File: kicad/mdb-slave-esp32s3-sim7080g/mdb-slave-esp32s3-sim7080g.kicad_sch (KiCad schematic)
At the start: 81 parts, among them J1 USB_C_Receptacle_USB2.0_16P, J2 JAE_SIM_Card_SF72S006, J3 Conn_01x03_Pin, J4 Conn_Coaxial, J5 Conn_Coaxial, J6 MDB_Connector, J7 Conn_01x03_Pin, J8 Conn_01x04_Pin, Q1 MMBT3904, Q2 MMBT3904, Q3 MMBT3904, Q4 MMBT3904, Q5 MMBT3904, Q6 MMBT3904, Q7 MMBT3904, SW1 SW_Push, U1 ESP32-S3FH4R2, U2 SIM7080G, U3 LM2594HVM-3.3, U4 TLP785, U5 TLP785, Y1 Crystal_GND24

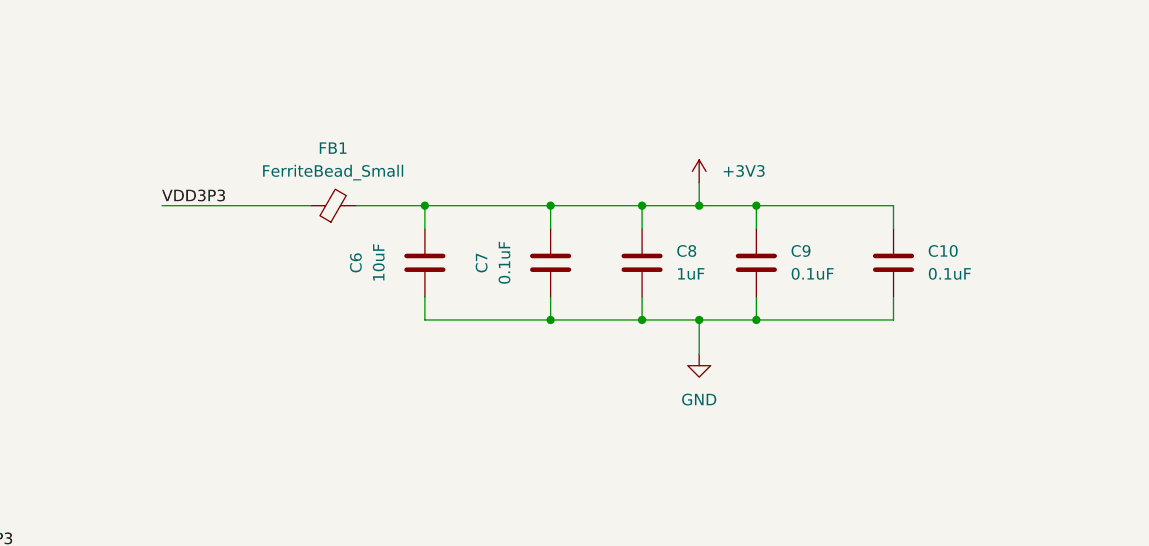
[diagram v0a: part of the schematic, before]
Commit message: moving capacitor 0.1uf to left ferrite bead
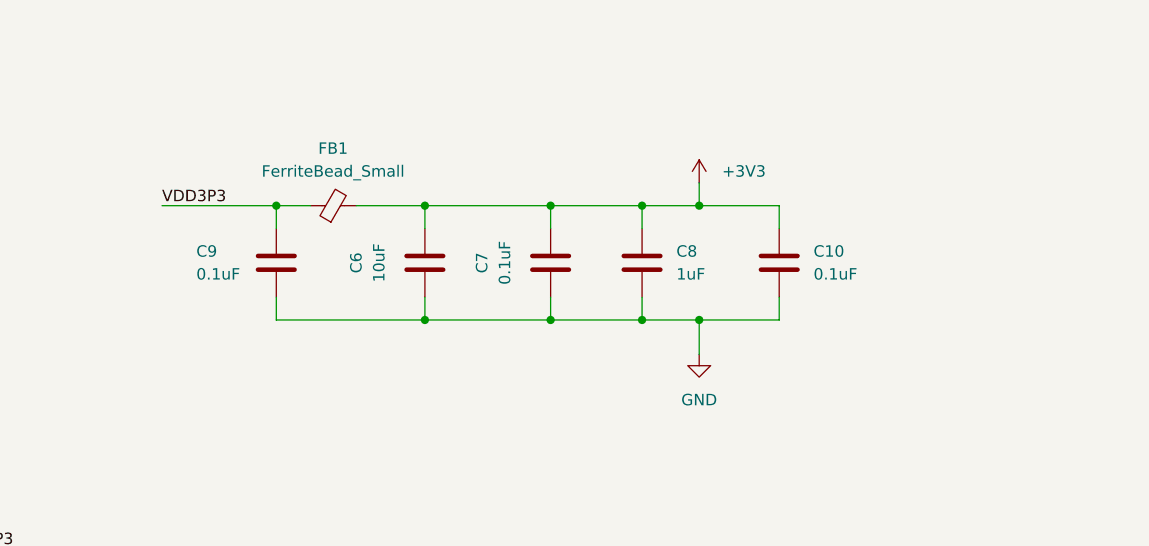
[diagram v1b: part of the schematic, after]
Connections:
- net +3V3: no longer C9.1
- net VDD3P3: now also C9.1
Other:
- moved on the sheet: C10, C9
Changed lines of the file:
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@@
 	)
 	(junction
-		(at 209.55 60.96)
-		(diameter 0)
-		(color 0 0 0 0)
-	)
-	(junction
 		(at 252.73 270.51)
 		(diameter 0)
@@
 	)
 	(junction
+		(at 172.72 60.96)
+		(diameter 0)
+		(color 0 0 0 0)
+	)
+	(junction
 		(at 81.28 133.35)
 		(diameter 0)
@@
 	)
 	(junction
-		(at 209.55 48.26)
-		(diameter 0)
-		(color 0 0 0 0)
-	)
-	(junction
 		(at 219.71 148.59)
 		(diameter 0)
@@
 	)
 	(junction
+		(at 156.21 48.26)
+		(diameter 0)
+		(color 0 0 0 0)
+	)
+	(junction
 		(at 63.5 123.19)
 		(diameter 0)
@@
 	(wire
 		(pts
-			(xy 224.79 48.26) (xy 224.79 50.8)
+			(xy 212.09 48.26) (xy 212.09 50.8)
 		)
 		(stroke
@@
 	(wire
 		(pts
-			(xy 209.55 60.96) (xy 224.79 60.96)
-		)
-		(stroke
-			(width 0)
-			(type default)
-		)
-	)
-	(wire
-		(pts
 			(xy 297.18 306.07) (xy 294.64 306.07)
 		)
@@
 	(wire
 		(pts
-			(xy 143.51 48.26) (xy 160.02 48.26)
+			(xy 143.51 48.26) (xy 156.21 48.26)
 		)
 		(stroke
@@
 	(wire
 		(pts
-			(xy 209.55 50.8) (xy 209.55 48.26)
+			(xy 156.21 48.26) (xy 156.21 50.8)
 		)
 		(stroke
@@
 	(wire
 		(pts
+			(xy 156.21 60.96) (xy 172.72 60.96)
+		)
+		(stroke
+			(width 0)
+			(type default)
+		)
+	)
+	(wire
+		(pts
 			(xy 81.28 147.32) (xy 81.28 144.78)
 		)
@@
 	(wire
 		(pts
+			(xy 156.21 58.42) (xy 156.21 60.96)
+		)
+		(stroke
+			(width 0)
+			(type default)
+		)
+	)
+	(wire
+		(pts
 			(xy 426.72 57.15) (xy 416.56 57.15)
 		)
@@
 	(wire
 		(pts
-			(xy 209.55 60.96) (xy 209.55 58.42)
-		)
-		(stroke
-			(width 0)
-			(type default)
-		)
-	)
-	(wire
-		(pts
 			(xy 26.67 109.22) (xy 26.67 115.57)
 		)
@@
 	(wire
 		(pts
-			(xy 203.2 60.96) (xy 209.55 60.96)
+			(xy 203.2 60.96) (xy 212.09 60.96)
 		)
 		(stroke
@@
 	(wire
 		(pts
+			(xy 156.21 48.26) (xy 160.02 48.26)
+		)
+		(stroke
+			(width 0)
+			(type default)
+		)
+	)
+	(wire
+		(pts
 			(xy 425.45 149.86) (xy 436.88 149.86)
 		)
@@
 	(wire
 		(pts
-			(xy 224.79 60.96) (xy 224.79 58.42)
+			(xy 212.09 60.96) (xy 212.09 58.42)
 		)
 		(stroke
@@
 	(wire
 		(pts
-			(xy 209.55 48.26) (xy 224.79 48.26)
-		)
-		(stroke
-			(width 0)
-			(type default)
-		)
-	)
-	(wire
-		(pts
 			(xy 105.41 243.84) (xy 105.41 248.92)
 		)
@@
 	(wire
 		(pts
-			(xy 203.2 48.26) (xy 209.55 48.26)
+			(xy 203.2 48.26) (xy 212.09 48.26)
 		)
 		(stroke
@@
 	(symbol
 		(lib_id "Device:C")
-		(at 224.79 54.61 0)
+		(at 212.09 54.61 0)
 		(unit 1)
 		(exclude_from_sim no)
@@
 		(fields_autoplaced yes)
 		(property "Reference" "C10"
-			(at 228.6 53.3399 0)
+			(at 215.9 53.3399 0)
 			(effects
 				(font
@@
 		)
 		(property "Value" "0.1uF"
-			(at 228.6 55.8799 0)
+			(at 215.9 55.8799 0)
 			(effects
 				(font
@@
 		)
 		(property "Footprint" "Capacitor_SMD:C_0603_1608Metric"
-			(at 225.7552 58.42 0)
+			(at 213.0552 58.42 0)
 			(effects
 				(font
@@
 		)
 		(property "Datasheet" "~"
-			(at 224.79 54.61 0)
+			(at 212.09 54.61 0)
 			(effects
 				(font
@@
 		)
 		(property "Description" ""
-			(at 224.79 54.61 0)
+			(at 212.09 54.61 0)
 			(effects
 				(font
@@
 		)
 		(property "LCSC#" "C5137636"
-			(at 224.79 54.61 90)
+			(at 212.09 54.61 90)
 			(effects
 				(font
@@
 		)
 		(property "Sim.Device" ""
-			(at 224.79 54.61 90)
+			(at 212.09 54.61 90)
 			(effects
 				(font
@@
 		)
 		(property "Sim.Pins" ""
-			(at 224.79 54.61 90)
+			(at 212.09 54.61 90)
 			(effects
 				(font
@@
 		)
 		(property "Sim.Type" ""
-			(at 224.79 54.61 90)
+			(at 212.09 54.61 90)
 			(effects
 				(font
@@
 	(symbol
 		(lib_id "Device:C")
-		(at 209.55 54.61 0)
+		(at 156.21 54.61 0)
 		(unit 1)
 		(exclude_from_sim no)
@@
 		(on_board yes)
 		(dnp no)
-		(fields_autoplaced yes)
 		(property "Reference" "C9"
-			(at 213.36 53.3399 0)
+			(at 147.32 53.34 0)
 			(effects
 				(font
@@
 		)
 		(property "Value" "0.1uF"
-			(at 213.36 55.8799 0)
+			(at 147.32 55.88 0)
 			(effects
 				(font
@@
 		)
 		(property "Footprint" "Capacitor_SMD:C_0603_1608Metric"
-			(at 210.5152 58.42 0)
+			(at 157.1752 58.42 0)
 			(effects
 				(font
@@
 		)
 		(property "Datasheet" "~"
-			(at 209.55 54.61 0)
+			(at 156.21 54.61 0)
 			(effects
 				(font
@@
 		)
 		(property "Description" ""
-			(at 209.55 54.61 0)
+			(at 156.21 54.61 0)
 			(effects
 				(font
@@
 		)
 		(property "LCSC#" "C5137636"
-			(at 209.55 54.61 90)
+			(at 156.21 54.61 90)
 			(effects
 				(font
@@
 		)
 		(property "Sim.Device" ""
-			(at 209.55 54.61 90)
+			(at 156.21 54.61 90)
 			(effects
 				(font
@@
 		)
 		(property "Sim.Pins" ""
-			(at 209.55 54.61 90)
+			(at 156.21 54.61 90)
 			(effects
 				(font
@@
 		)
 		(property "Sim.Type" ""
-			(at 209.55 54.61 90)
+			(at 156.21 54.61 90)
 			(effects
 				(font

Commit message: initial updates
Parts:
- removed R27: 4K7, Resistor_SMD:R_0603_1608Metric, symbol Device:R
- added Q9: MMBT3904, Package_TO_SOT_SMD:SOT-23, symbol Transistor_BJT:MMBT3904
- added R26, R29: 1k, Resistor_SMD:R_0603_1608Metric, symbol Device:R
- added R28, R30: 10k, Resistor_SMD:R_0603_1608Metric, symbol Device:R
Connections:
- net +3V3: now also R29.1, R30.2
- net GND: now also R28.1
- net io13: now also R26.2
- net io6: now also Q9.3 (C), R29.2
- net at Q7.1 (B): now also R26.1, R28.2
- net pulse: now reaches J7.3 (Pin_3), Q7.3 (C)
- net pulse: now also Q9.2 (E)
- new net: Q9.1 (B), R30.1
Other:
- moved on the sheet: J7, Q7

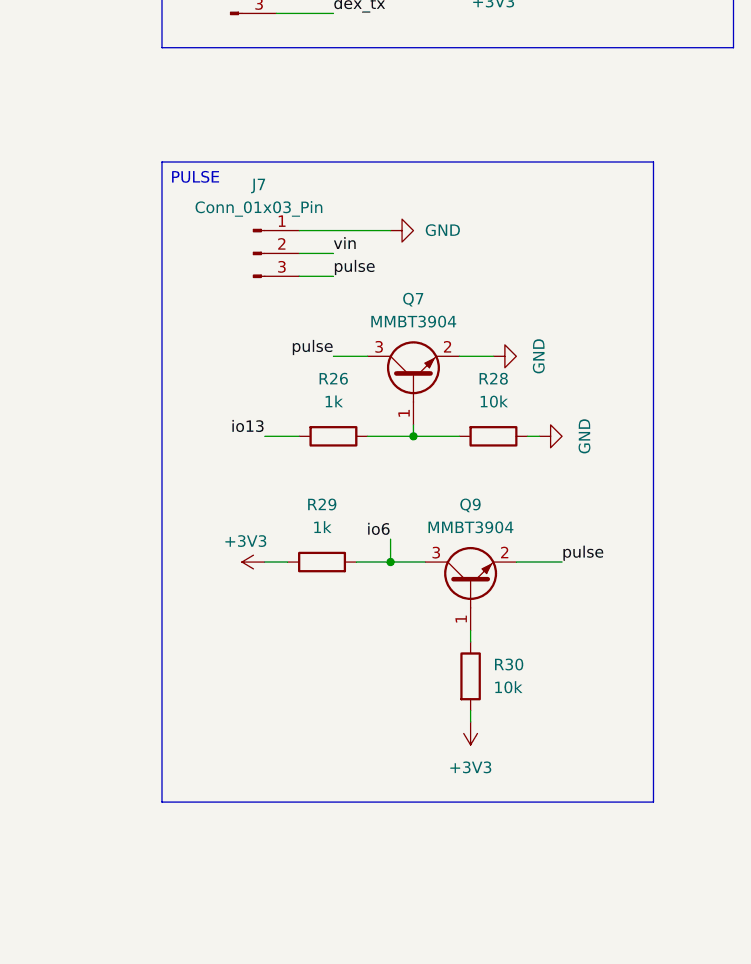
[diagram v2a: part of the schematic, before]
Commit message: routing pulse rx
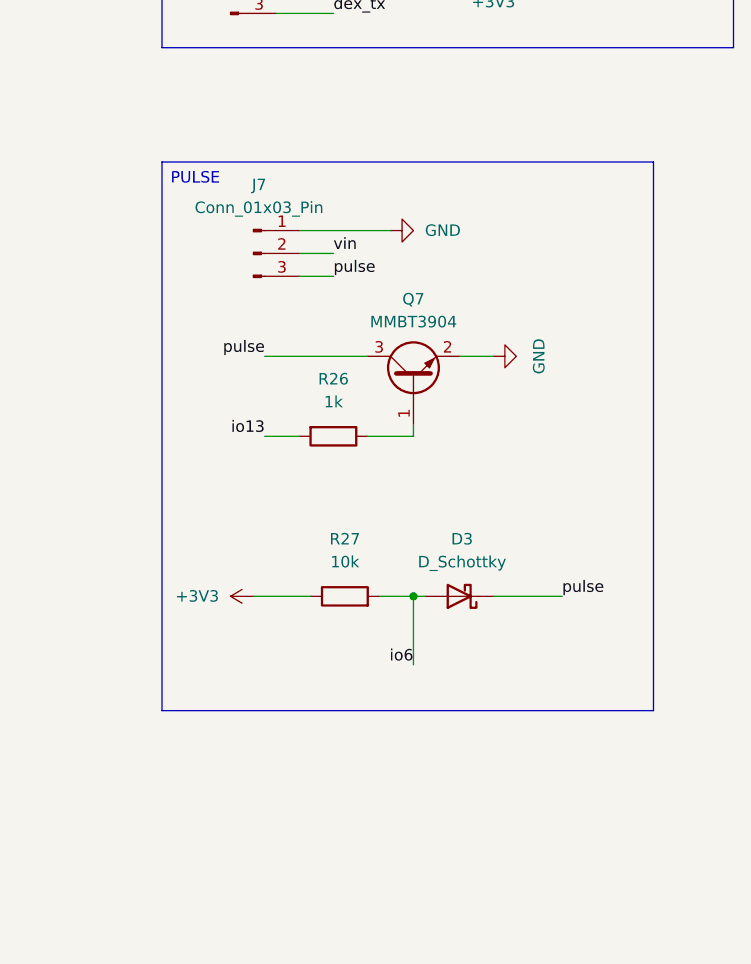
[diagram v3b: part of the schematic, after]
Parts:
- removed Q9: MMBT3904, Package_TO_SOT_SMD:SOT-23, symbol Transistor_BJT:MMBT3904
- removed R28, R30: 10k, Resistor_SMD:R_0603_1608Metric, symbol Device:R
- removed R29: 1k, Resistor_SMD:R_0603_1608Metric, symbol Device:R
- added D3: D_Schottky, Diode_SMD:D_SOD-123, symbol Device:D_Schottky
- added R27: 10k, Resistor_SMD:R_0603_1608Metric, symbol Device:R
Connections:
- net +3V3: now also R27.1
- net io6: now also D3.2 (A), R27.2
- net pulse: now also D3.1 (K)
